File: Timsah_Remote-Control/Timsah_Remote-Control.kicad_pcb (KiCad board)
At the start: 2 copper layers, 200 x 100 mm, 45 parts, among them J1 Güç Girişi, J2 ICSP, J3 Klemens, SW1 Oto Depth, SW10 Backward, SW2 Lights, SW3 Up, SW4 Down, SW5 Power, SW6 Turn Back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

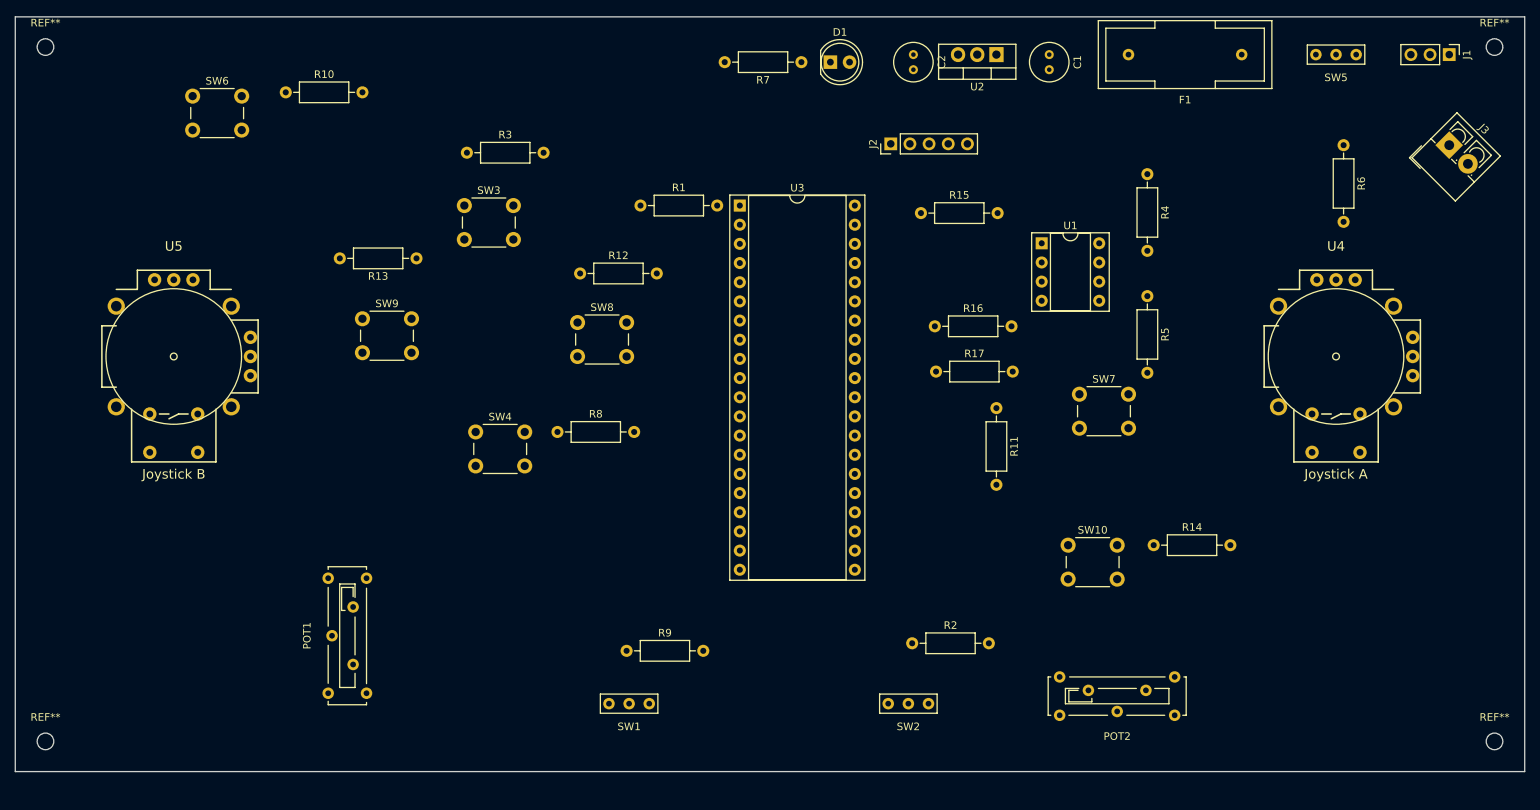
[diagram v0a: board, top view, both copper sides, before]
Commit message: Added remote controle PCB design.
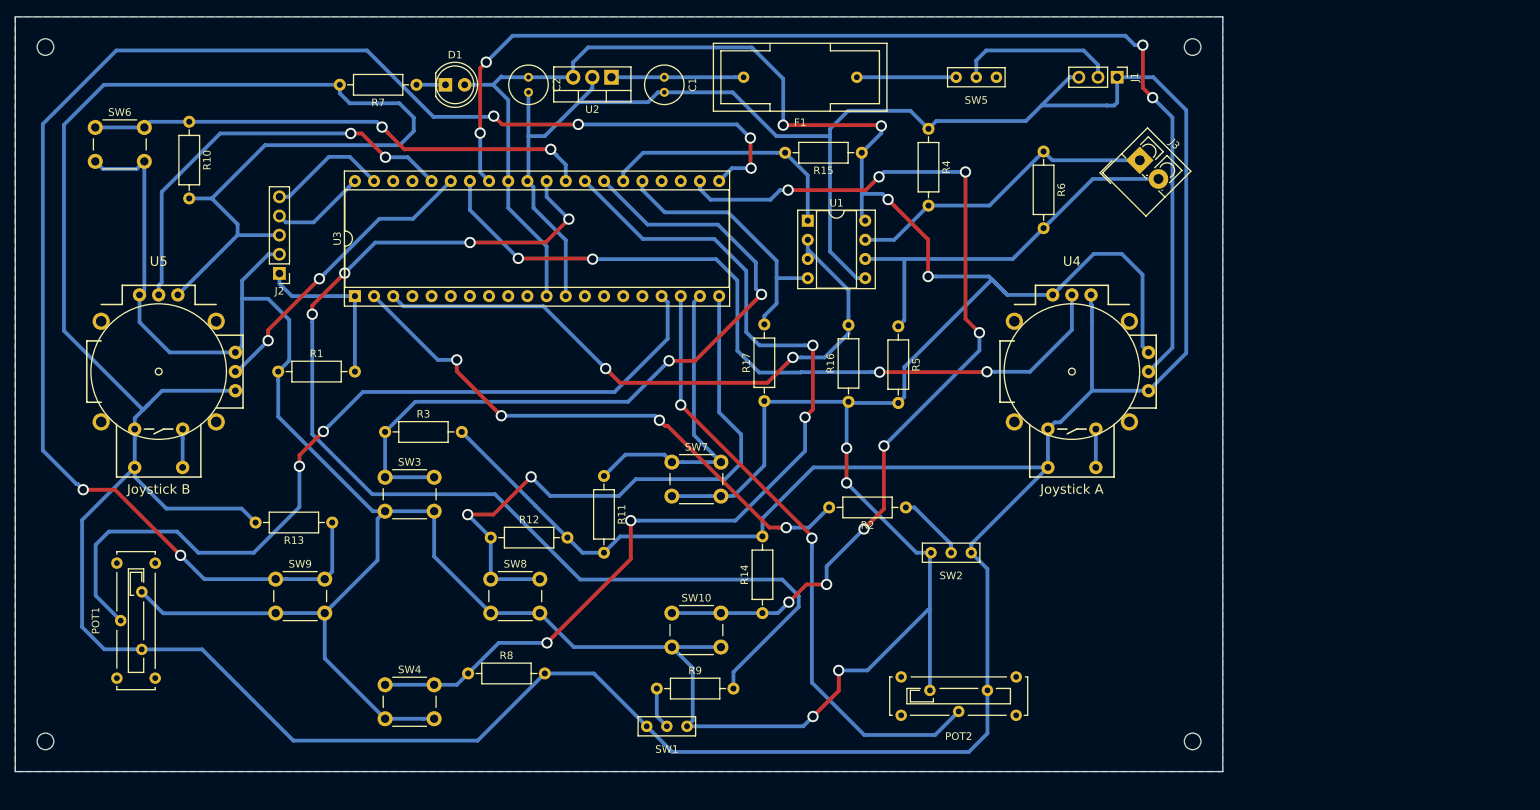
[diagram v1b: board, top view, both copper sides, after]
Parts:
- moved J2 82.8 mm to (80.0, 79.0), turned to 180 degrees
- moved SW7 54.7 mm to (132.0, 104.0)
- moved SW10 53.3 mm to (132.0, 124.0)
- moved R1 52.8 mm to (79.8, 92.0)
- moved R11 52.8 mm to (123.0, 105.8)
- moved R14 52.6 mm to (144.0, 124.0), turned to 90 degrees
- moved U3 52.4 mm to (90.0, 82.0), turned to 90 degrees
- moved C1 51.1 mm to (131.0, 53.0)
- moved C2 51.1 mm to (113.0, 53.0)
- moved D1 51.1 mm to (102.0, 54.0)
- moved F1 51.1 mm to (149.0, 53.0)
- moved R7 51.1 mm to (98.2, 54.0)
- moved U2 51.1 mm to (124.0, 53.0)
- moved SW5 47.8 mm to (172.3, 53.0)
- moved J1 44.1 mm to (191.0, 53.0)
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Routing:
- net GND: track 0.00 -> 718.7 mm
- net +5V: track 0.00 -> 552.9 mm, vias 0 -> 8
- net Left: track 0.00 -> 207.2 mm, vias 0 -> 6
- net VRX-A: track 0.00 -> 151.7 mm, vias 0 -> 4
- net OTO_DEPTH: track 0.00 -> 151.2 mm, vias 0 -> 4
- net Down: track 0.00 -> 129.9 mm, vias 0 -> 4
- net Backward: track 0.00 -> 124.2 mm, vias 0 -> 8
- net SERVO_Cam: track 0.00 -> 110.8 mm, vias 0 -> 2
- net VRY-A: track 0.00 -> 104.9 mm, vias 0 -> 4
- net Up: track 0.00 -> 99.0 mm, vias 0 -> 2
- net ENABLE: track 0.00 -> 83.7 mm, vias 0 -> 2
- net SERVO_Grip: track 0.00 -> 82.0 mm, vias 0 -> 2
- net Right: track 0.00 -> 80.8 mm, vias 0 -> 2
- net SW: track 0.00 -> 75.0 mm, vias 0 -> 4
- net TURN_BACK: track 0.00 -> 67.2 mm, vias 0 -> 2
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- added copper zone on B.Cu, net GND
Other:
- board size 200 x 100 mm -> 160 x 100 mm
- net class Default: clearance 0.2 -> 0.3; trace_width 0.25 -> 0.5; via_dia 0.8 -> 1.5; via_drill 0.4 -> 1
- rule trace_clearance: 0.2 -> 0.3

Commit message: Remote control board recreated.
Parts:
- removed REF** (x4): MountingHole_2.2mm_M2, MountingHole:MountingHole_2.2mm_M2
- added D2: LED, LED_THT:LED_D5.0mm, F.Cu at (99.7, 58.9)
- added R18: 1k, Resistor_THT:R_Axial_DIN0207_L6.3mm_D2.5mm_P10.16mm_Horizontal, F.Cu at (89.5, 52.0)
- moved U5 147.9 mm to (211.8, 95.8)
- moved U4 93.9 mm to (91.2, 95.8)
- moved R1 93.3 mm to (172.6, 81.8), turned to 180 degrees
- moved J2 93.2 mm to (172.6, 89.8), turned to 0 degrees
- moved SW1 77.0 mm to (159.8, 67.4)
- moved U3 72.7 mm to (162.5, 87.2), turned to 270 degrees
- moved SW4 72.0 mm to (125.4, 68.8), turned to 180 degrees
- moved R9 67.8 mm to (160.1, 73.2), turned to 180 degrees
- moved J3 63.5 mm to (222.1, 121.0)
- moved R8 62.5 mm to (126.8, 73.4), turned to 180 degrees
- moved POT1 61.0 mm to (83.8, 68.4)
- moved R4 58.2 mm to (189.2, 113.2), turned to 180 degrees
- moved SW3 58.1 mm to (138.6, 68.8), turned to 180 degrees
- moved SW2 52.8 mm to (189.7, 67.4)
- moved R6 52.4 mm to (197.1, 112.8)
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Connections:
- R4 pad 1: GND -> +5V
- U3 pad 10: Net-(U3-Pad10) -> Down
- U3 pad 15: Net-(U3-Pad15) -> VRX-A
- U3 pad 16: Net-(U3-Pad16) -> VRY-A
- U3 pad 17: SERVO_Cam -> LED
- U3 pad 18: SERVO_Grip -> TURN_BACK
- U3 pad 19: Forward -> Net-(U3-Pad19)
- U3 pad 2: SW -> Net-(U3-Pad2)
- U3 pad 20: Right -> SERVO_Cam
- U3 pad 23: Net-(U3-Pad23) -> Forward
- U3 pad 24: Net-(U3-Pad24) -> Right
- U3 pad 27: Up -> Net-(U3-Pad27)
- U3 pad 28: Down -> Net-(U3-Pad28)
- U3 pad 29: TURN_BACK -> Net-(U3-Pad29)
- U3 pad 3: ENABLE -> SW
- U3 pad 30: OTO_DEPTH -> Net-(U3-Pad30)
- U3 pad 33: VRX-A -> Net-(U3-Pad33)
- U3 pad 34: VRY-A -> Net-(U3-Pad34)
- U3 pad 35: VRX-B -> SERVO_Grip
- U3 pad 36: VRY-B -> ENABLE
- U3 pad 37: Net-(U3-Pad37) -> VRX-B
- U3 pad 38: Net-(U3-Pad38) -> VRY-B
- U3 pad 4: Net-(U3-Pad4) -> OTO_DEPTH
- U3 pad 9: Net-(U3-Pad9) -> Up
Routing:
- net GND: track 718.7 -> 76.7 mm, vias 0 -> 6
- net Left: track 207.2 -> 36.9 mm, vias 6 -> 0
- net OTO_DEPTH: track 151.2 -> 16.1 mm, vias 4 -> 0
- net VRX-A: track 151.7 -> 32.4 mm, vias 4 -> 0
- net Down: track 129.9 -> 33.2 mm, vias 4 -> 0
- net SERVO_Cam: track 110.8 -> 40.3 mm, vias 2 -> 0
- net Up: track 99.0 -> 32.6 mm, vias 2 -> 0
- net Backward: track 124.2 -> 58.0 mm, vias 8 -> 0
- net VRY-A: track 104.9 -> 43.2 mm, vias 4 -> 0
- net Right: track 80.8 -> 31.7 mm, vias 2 -> 0
- net +5V: track 552.9 -> 596.0 mm, vias 8 -> 12
- net SW: track 75.0 -> 32.1 mm, vias 4 -> 0
- net LED: track 0.00 -> 39.3 mm
- net ENABLE: track 83.7 -> 45.6 mm, vias 2 -> 0
- net SERVO_Grip: track 82.0 -> 45.0 mm
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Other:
- board text added: "Timsah - BTU ROV Remote Controller 09.08.2019"
- board text added: "v1.0"

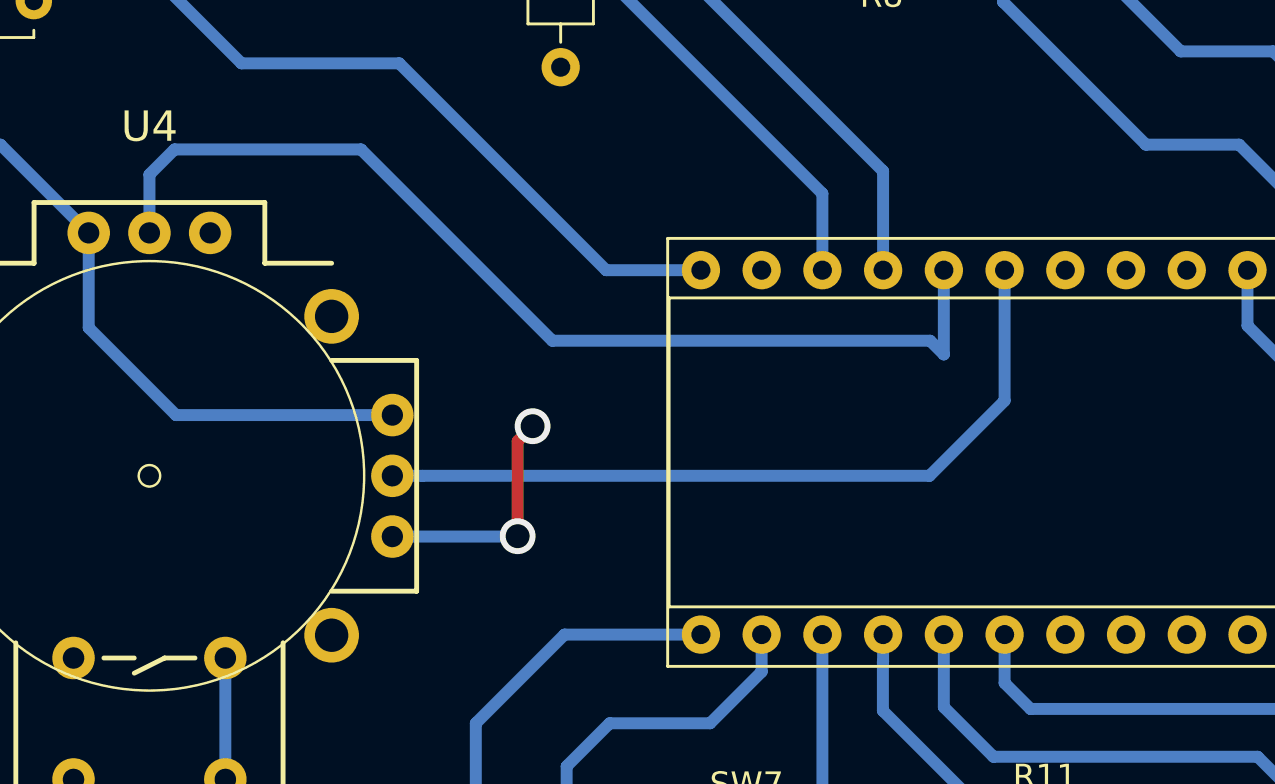
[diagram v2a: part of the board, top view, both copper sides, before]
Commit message: Remote controller joystick pins changed.
Joystick A pins do not connected to analog pins.
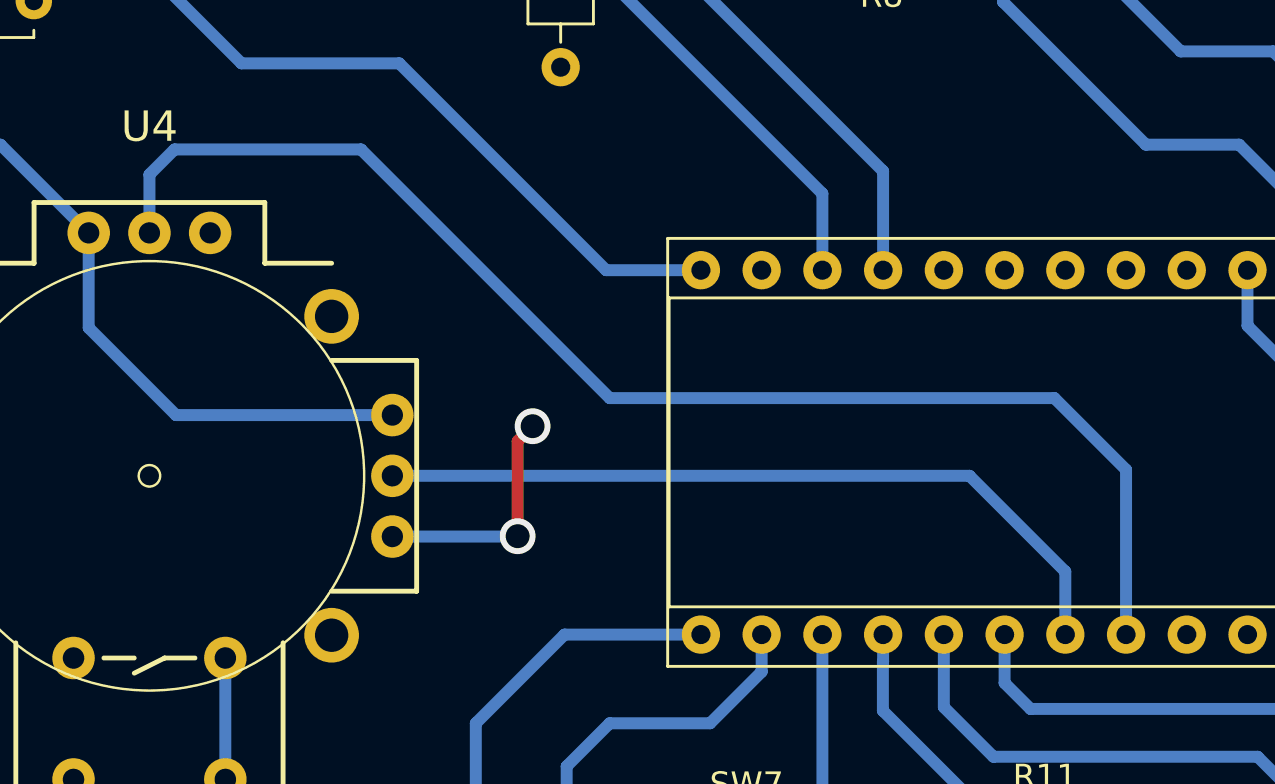
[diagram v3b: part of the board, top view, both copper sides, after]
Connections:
- U3 pad 15: VRX-A -> Net-(U3-Pad15)
- U3 pad 16: VRY-A -> Net-(U3-Pad16)
- U3 pad 27: Net-(U3-Pad27) -> VRX-A
- U3 pad 28: Net-(U3-Pad28) -> VRY-A
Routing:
- net VRY-A: track 43.2 -> 56.2 mm

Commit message: Hardware Update
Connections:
- R4 pad 1: +5V -> GND
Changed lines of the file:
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@@
     (thickness 1.6)
     (drawings 8)
-    (tracks 362)
+    (tracks 361)
     (zones 0)
     (modules 43)
@@
       (net 10 "Net-(J3-Pad1)"))
     (pad 1 thru_hole circle (at 0 0 180) (size 1.6 1.6) (drill 0.8) (layers *.Cu *.Mask)
-      (net 3 +5V))
+      (net 2 GND))
     (model ${KISYS3DMOD}/Resistor_THT.3dshapes/R_Axial_DIN0207_L6.3mm_D2.5mm_P10.16mm_Horizontal.wrl
       (at (xyz 0 0 0))
@@
   (segment (start 189.175 123.73137) (end 174.35637 138.55) (width 0.5) (layer B.Cu) (net 3))
   (segment (start 189.175 122.6) (end 189.175 123.73137) (width 0.5) (layer B.Cu) (net 3) (status 10))
-  (segment (start 189.175 112.04363) (end 185.43137 108.3) (width 0.5) (layer B.Cu) (net 3))
-  (segment (start 189.175 113.175) (end 189.175 112.04363) (width 0.5) (layer B.Cu) (net 3) (status 10))
   (segment (start 178.595 108.3) (end 172.845 114.05) (width 0.5) (layer B.Cu) (net 3) (status 20))
   (segment (start 185.43137 108.3) (end 178.595 108.3) (width 0.5) (layer B.Cu) (net 3))
@@
   (segment (start 166.925 67.4) (end 162.425 67.4) (width 0.5) (layer B.Cu) (net 3) (status 20))
   (segment (start 169.825 70.3) (end 166.925 67.4) (width 0.5) (layer B.Cu) (net 3))
-  (via (at 192.5 122.525) (size 1.5) (drill 1) (layers F.Cu B.Cu) (net 3))
-  (segment (start 189.175 122.6) (end 192.425 122.6) (width 0.5) (layer B.Cu) (net 3) (status 10))
-  (segment (start 192.425 122.6) (end 192.5 122.525) (width 0.5) (layer B.Cu) (net 3))
-  (via (at 192.5 113.15) (size 1.5) (drill 1) (layers F.Cu B.Cu) (net 3))
-  (segment (start 192.5 122.525) (end 192.5 113.15) (width 0.5) (layer F.Cu) (net 3))
-  (segment (start 189.2 113.15) (end 189.175 113.175) (width 0.5) (layer B.Cu) (net 3) (status 30))
-  (segment (start 192.5 113.15) (end 189.2 113.15) (width 0.5) (layer B.Cu) (net 3) (status 20))
   (segment (start 133.4 54) (end 138.55 59.15) (width 0.5) (layer B.Cu) (net 3))
   (segment (start 130.315 54) (end 133.4 54) (width 0.5) (layer B.Cu) (net 3) (status 10))
@@
   (segment (start 88.61 85.69) (end 84.92 82) (width 0.5) (layer B.Cu) (net 3) (status 10))
   (segment (start 84.92 82) (end 79.625 82) (width 0.5) (layer B.Cu) (net 3))
+  (segment (start 192.5 122.525) (end 192.5 113.15) (width 0.5) (layer F.Cu) (net 3))
+  (segment (start 192.425 122.6) (end 192.5 122.525) (width 0.5) (layer B.Cu) (net 3))
+  (segment (start 189.175 122.6) (end 192.425 122.6) (width 0.5) (layer B.Cu) (net 3) (status 10))
+  (via (at 192.5 113.15) (size 1.5) (drill 1) (layers F.Cu B.Cu) (net 3))
+  (via (at 192.5 122.525) (size 1.5) (drill 1) (layers F.Cu B.Cu) (net 3))
+  (segment (start 188.14203 107.73137) (end 186 107.73137) (width 0.5) (layer B.Cu) (net 3))
+  (segment (start 192.5 112.08934) (end 188.14203 107.73137) (width 0.5) (layer B.Cu) (net 3))
+  (segment (start 192.5 113.15) (end 192.5 112.08934) (width 0.5) (layer B.Cu) (net 3))
   (segment (start 127.75 53.975) (end 127.775 54) (width 0.5) (layer B.Cu) (net 4) (status 30))
   (segment (start 124.025 53.975) (end 127.75 53.975) (width 0.5) (layer B.Cu) (net 4) (status 30))
@@
   (segment (start 124.375 102.49) (end 124.375 105.525) (width 0.5) (layer B.Cu) (net 27) (status 10))
   (segment (start 124.375 105.525) (end 126.45 107.6) (width 0.5) (layer B.Cu) (net 27))
-  (segment (start 129.455 99.855) (end 129.455 102.49) (width 0.5) (layer B.Cu) (net 32))
-  (segment (start 101.31 95.85) (end 125.45 95.85) (width 0.5) (layer B.Cu) (net 32))
+  (segment (start 129.455 99.855) (end 129.455 102.49) (width 0.5) (layer B.Cu) (net 32) (status 20))
+  (segment (start 101.31 95.85) (end 125.45 95.85) (width 0.5) (layer B.Cu) (net 32) (status 10))
   (segment (start 125.45 95.85) (end 129.455 99.855) (width 0.5) (layer B.Cu) (net 32))
-  (segment (start 131.995 95.595) (end 131.995 102.49) (width 0.5) (layer B.Cu) (net 34))
+  (segment (start 131.995 95.595) (end 131.995 102.49) (width 0.5) (layer B.Cu) (net 34) (status 20))
   (segment (start 91.15 83.25) (end 92.2 82.2) (width 0.5) (layer B.Cu) (net 34))
-  (segment (start 91.15 85.69) (end 91.15 83.25) (width 0.5) (layer B.Cu) (net 34))
+  (segment (start 91.15 85.69) (end 91.15 83.25) (width 0.5) (layer B.Cu) (net 34) (status 10))
   (segment (start 92.2 82.2) (end 100 82.2) (width 0.5) (layer B.Cu) (net 34))
   (segment (start 100 82.2) (end 110.4 92.6) (width 0.5) (layer B.Cu) (net 34))
